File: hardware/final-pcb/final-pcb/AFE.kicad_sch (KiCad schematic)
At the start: 1 part, among them U1 ADS1299-4PAGR

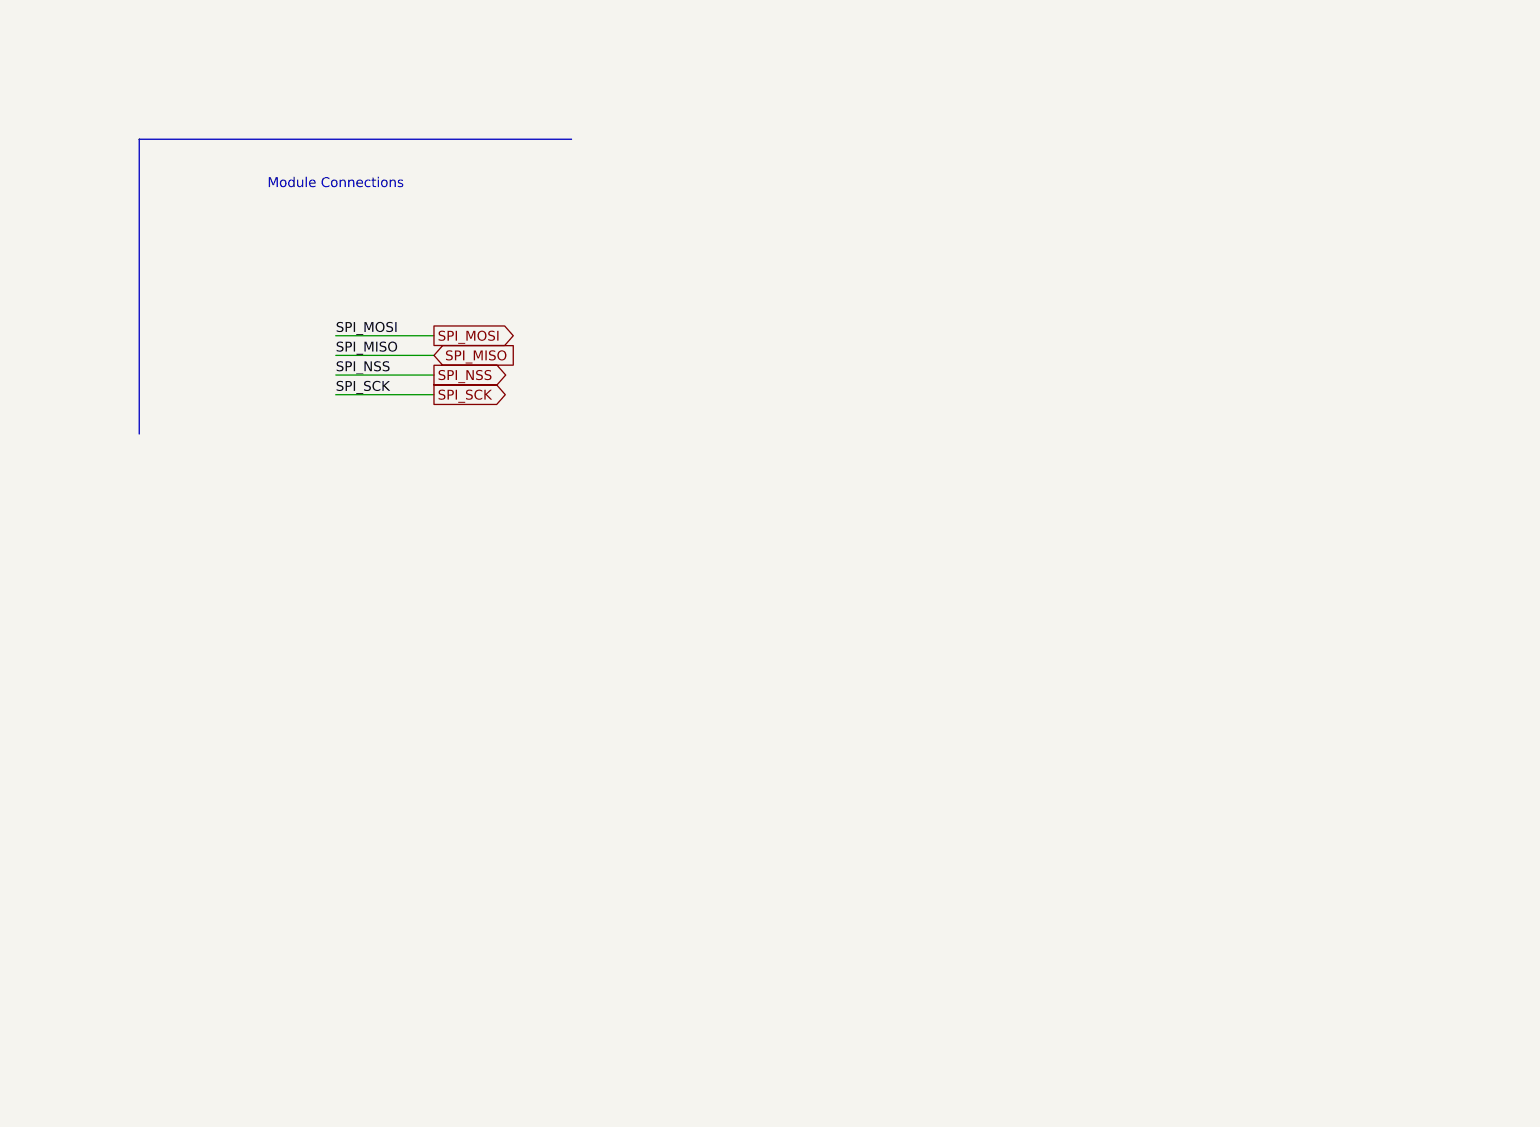
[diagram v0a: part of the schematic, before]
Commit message: Update sizes of schematics
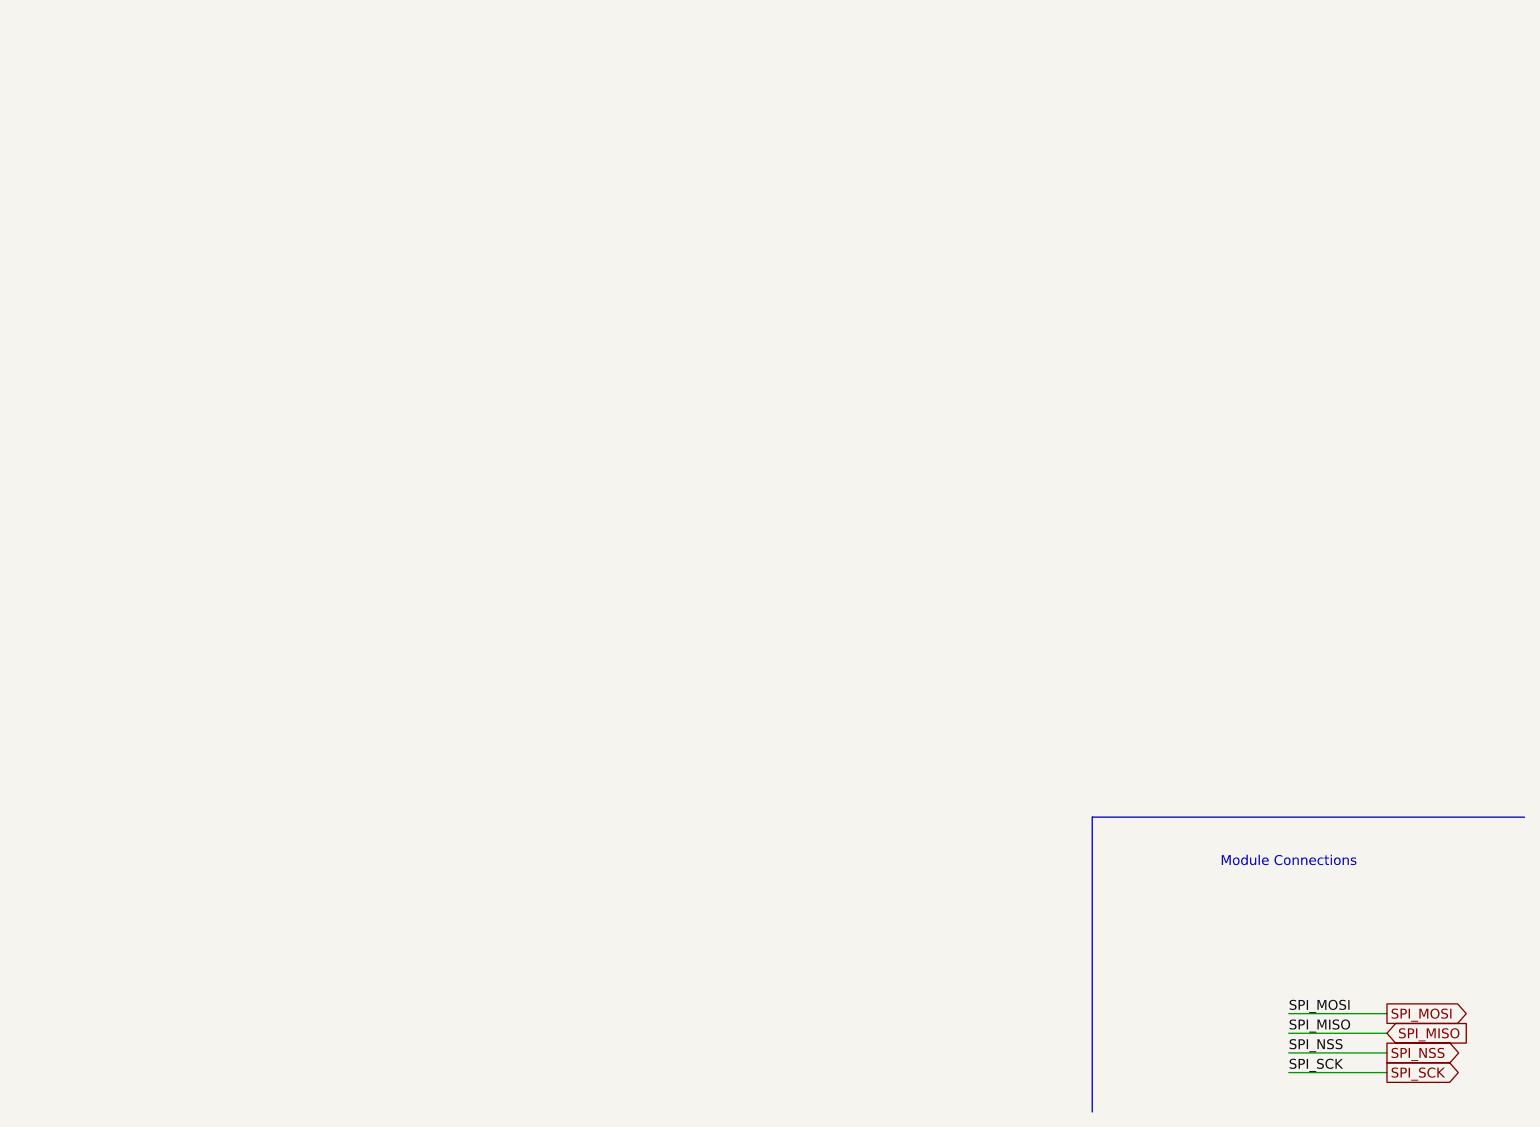
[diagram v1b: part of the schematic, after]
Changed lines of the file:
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@@
 	(generator "eeschema")
 	(generator_version "8.0")
-	(paper "A4")
+	(paper "A3")
 	(wire
 		(pts
@@
 	(polyline
 		(pts
-			(xy 228.6 127) (xy 228.6 165.1)
+			(xy 351.79 214.63) (xy 351.79 252.73)
 		)
 		(stroke
@@
 	(wire
 		(pts
-			(xy 254 157.48) (xy 266.7 157.48)
+			(xy 377.19 245.11) (xy 389.89 245.11)
 		)
 		(stroke
@@
 	(polyline
 		(pts
-			(xy 284.48 127) (xy 228.6 127)
+			(xy 407.67 214.63) (xy 351.79 214.63)
 		)
 		(stroke
@@
 	(wire
 		(pts
-			(xy 254 152.4) (xy 266.7 152.4)
+			(xy 377.19 240.03) (xy 389.89 240.03)
 		)
 		(stroke
@@
 	(wire
 		(pts
-			(xy 254 160.02) (xy 266.7 160.02)
+			(xy 377.19 247.65) (xy 389.89 247.65)
 		)
 		(stroke
@@
 	(wire
 		(pts
-			(xy 254 154.94) (xy 266.7 154.94)
+			(xy 377.19 242.57) (xy 389.89 242.57)
 		)
 		(stroke
@@
 	(text "Module Connections"
 		(exclude_from_sim no)
-		(at 254 132.842 0)
+		(at 377.19 220.472 0)
 		(effects
 			(font
@@
 	)
 	(label "SPI_MOSI"
-		(at 254 152.4 0)
+		(at 377.19 240.03 0)
 		(fields_autoplaced yes)
 		(effects
@@
 	)
 	(label "SPI_SCK"
-		(at 254 160.02 0)
+		(at 377.19 247.65 0)
 		(fields_autoplaced yes)
 		(effects
@@
 	)
 	(label "SPI_MISO"
-		(at 254 154.94 0)
+		(at 377.19 242.57 0)
 		(fields_autoplaced yes)
 		(effects
@@
 	)
 	(label "SPI_NSS"
-		(at 254 157.48 0)
+		(at 377.19 245.11 0)
 		(fields_autoplaced yes)
 		(effects
@@
 	(global_label "SPI_MISO"
 		(shape input)
-		(at 266.7 154.94 0)
+		(at 389.89 242.57 0)
 		(fields_autoplaced yes)
 		(effects
@@
 		)
 		(property "Intersheetrefs" "${INTERSHEET_REFS}"
-			(at 278.3333 154.94 0)
+			(at 401.5233 242.57 0)
 			(effects
 				(font
@@
 	(global_label "SPI_SCK"
 		(shape output)
-		(at 266.7 160.02 0)
+		(at 389.89 247.65 0)
 		(fields_autoplaced yes)
 		(effects
@@
 		)
 		(property "Intersheetrefs" "${INTERSHEET_REFS}"
-			(at 277.4866 160.02 0)
+			(at 400.6766 247.65 0)
 			(effects
 				(font
@@
 	(global_label "SPI_NSS"
 		(shape output)
-		(at 266.7 157.48 0)
+		(at 389.89 245.11 0)
 		(fields_autoplaced yes)
 		(effects
@@
 		)
 		(property "Intersheetrefs" "${INTERSHEET_REFS}"
-			(at 277.4866 157.48 0)
+			(at 400.6766 245.11 0)
 			(effects
 				(font
@@
 	(global_label "SPI_MOSI"
 		(shape output)
-		(at 266.7 152.4 0)
+		(at 389.89 240.03 0)
 		(fields_autoplaced yes)
 		(effects
@@
 		)
 		(property "Intersheetrefs" "${INTERSHEET_REFS}"
-			(at 278.3333 152.4 0)
+			(at 401.5233 240.03 0)
 			(effects
 				(font

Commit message: Add syms, footprints, 3dmodels for ADS and LTC boards
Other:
- company: (none) -> San Diego State University
- title: (none) -> EMG Analog Front End
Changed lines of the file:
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@@
 	(generator_version "8.0")
 	(paper "A3")
+	(title_block
+		(title "EMG Analog Front End")
+		(date "2025-03-01")
+		(company "San Diego State University")
+		(comment 1 "Computer Engineer: Noah Marosok, Blake Pearson")
+		(comment 2 "Electrical Engineer: Kelly Hubbard, Jayden Sumbillo, Kirk Young")
+	)
 	(wire
 		(pts
